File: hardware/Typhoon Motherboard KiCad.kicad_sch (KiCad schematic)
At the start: 51 parts, among them J1 Conn_01x04_Pin, J2 Conn_02x03_Odd_Even, J3 Conn_01x04_Pin, J4 Conn_01x02_Pin, J5 Conn_01x02_Pin, J6 Conn_01x02_Pin, J7 Conn_01x02_Pin, J8 Conn_01x02_Pin, J9 Conn_01x02_Pin, P1 USB_C_Plug_USB2.0, U1 ESP32-S3-WROOM-1, U2 TPS54331DDA, U3 TJA1051T-3, U7 MCP1825S

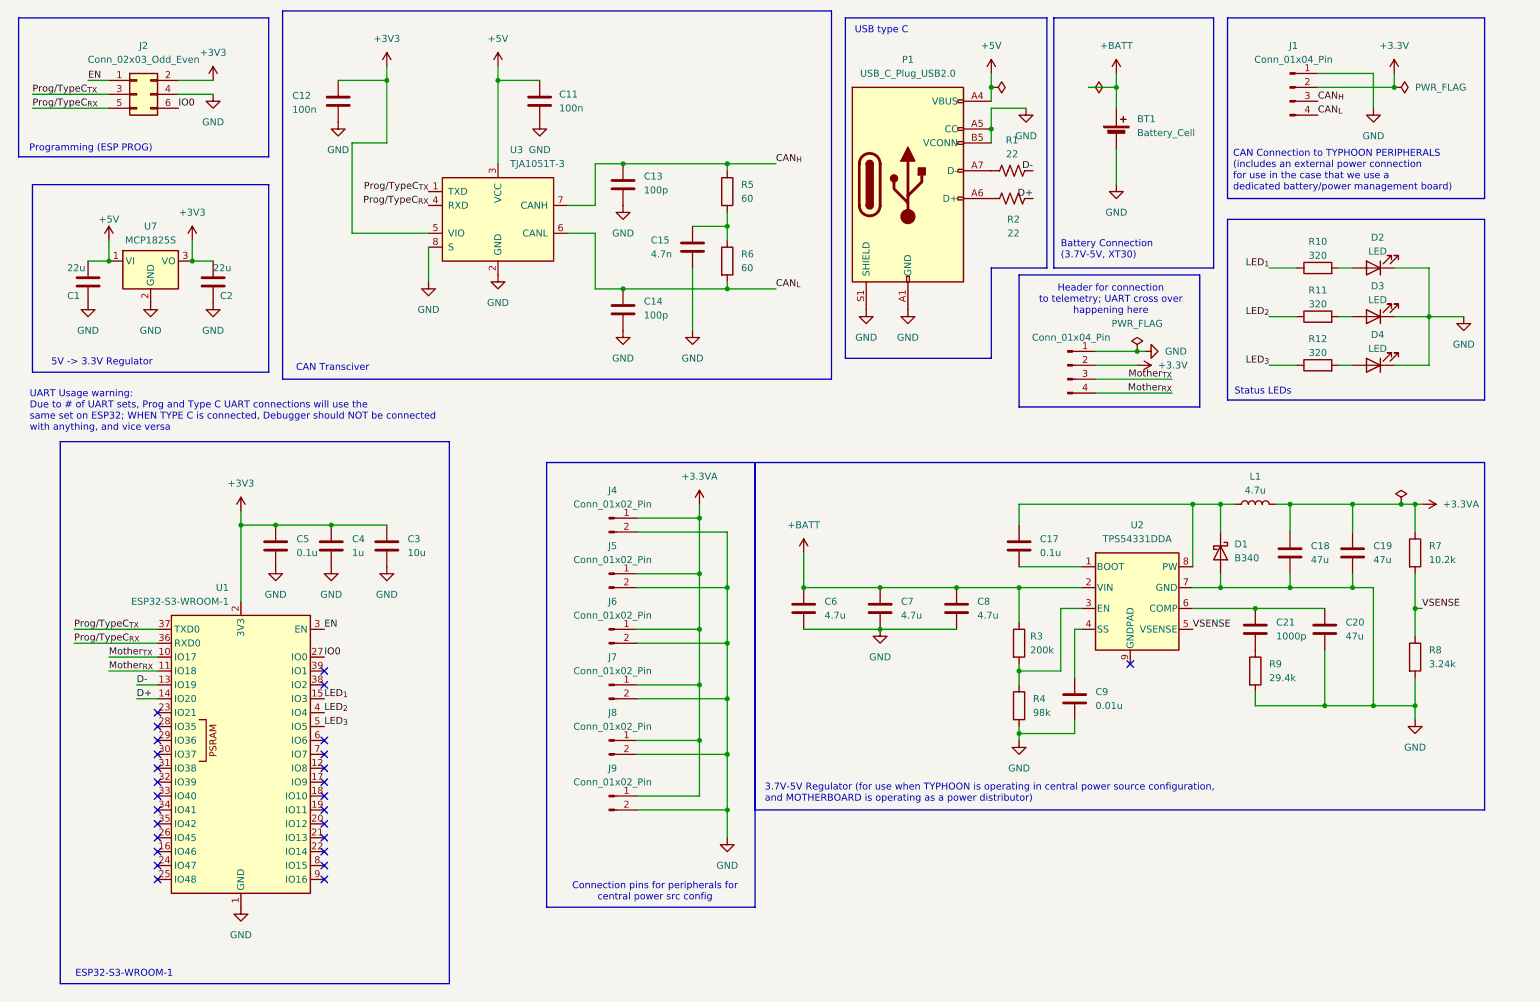
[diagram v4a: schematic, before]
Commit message: create new sheet; update USBC
created new sheet for the central power source configuration so it's more organized; updated the USB-C symbol; added in safety regulations (diodes) to prevent conflict in voltages
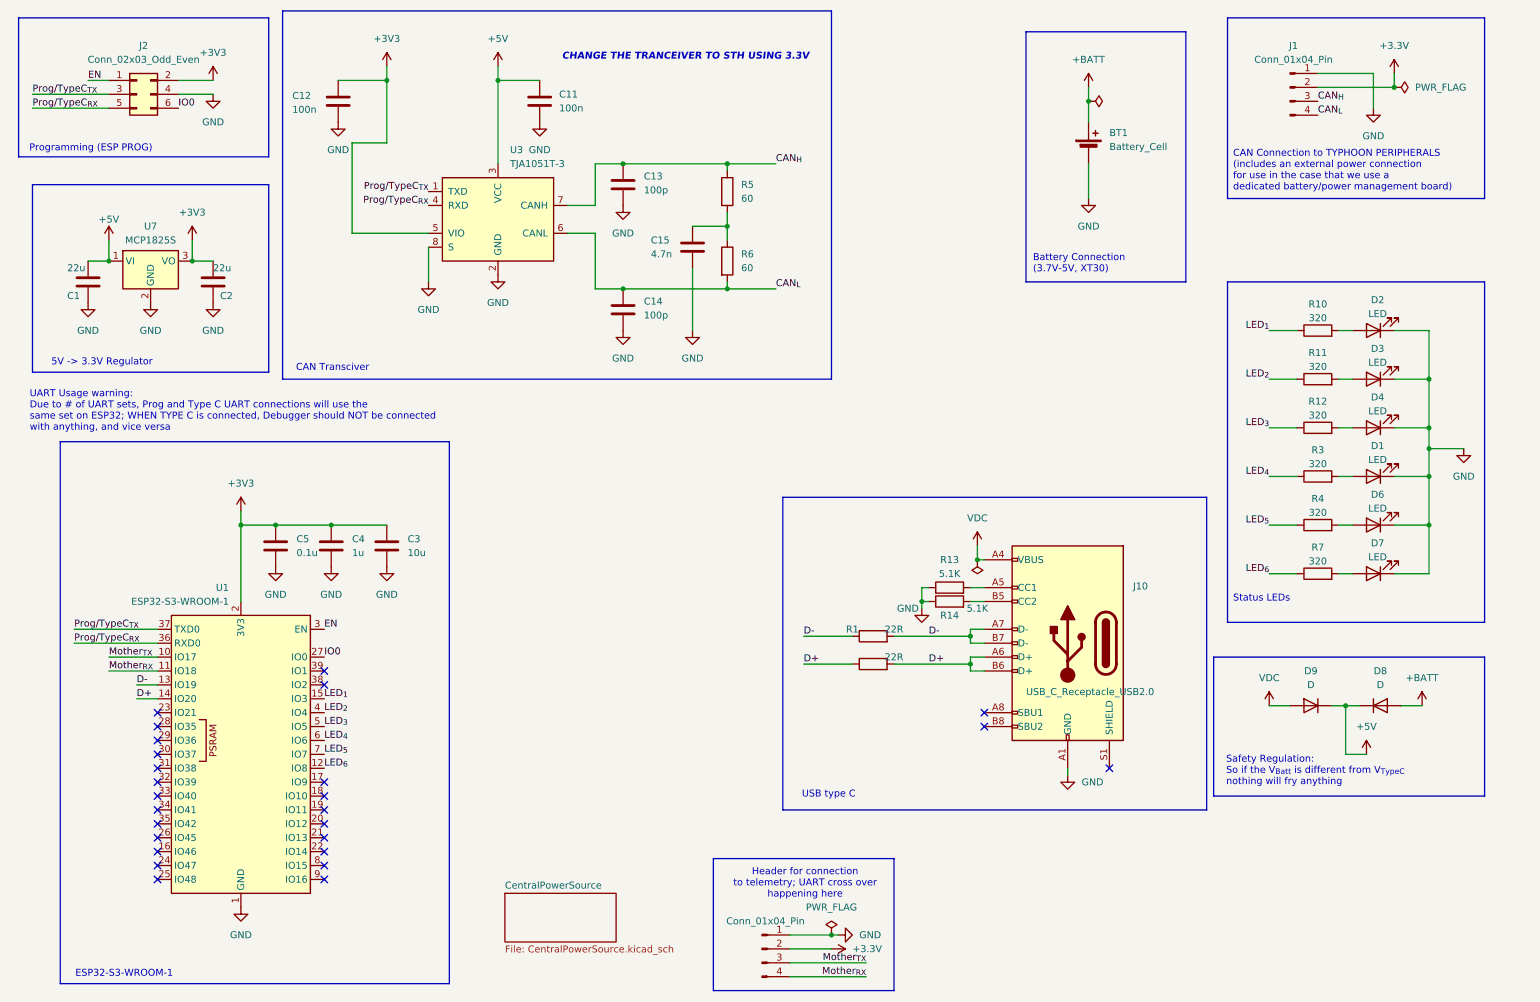
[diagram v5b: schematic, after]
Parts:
- removed C17: 0.1u, Capacitor_SMD:C_0603_1608Metric, symbol Device:C
- removed C18, C19, C20: 47u, Capacitor_SMD:C_0603_1608Metric, symbol Device:C
- removed C21: 1000p, Capacitor_SMD:C_0603_1608Metric, symbol Device:C
- removed C6, C7, C8: 4.7u, Capacitor_SMD:C_0603_1608Metric, symbol Device:C
- removed C9: 0.01u, Capacitor_SMD:C_0603_1608Metric, symbol Device:C
- removed D1: B340, Diode_SMD:D_SMC, symbol Diode:B340
- removed J4, J5, J6, J7, J8, J9: Conn_01x02_Pin, Connector_PinHeader_2.00mm:PinHeader_1x02_P2.00mm_Vertical_SMD_Pin1Right, symbol Connector:Conn_01x02_Pin
- removed L1: 4.7u, Inductor_SMD:L_Taiyo-Yuden_NR-60xx, symbol Device:L
- removed P1: USB_C_Plug_USB2.0, symbol Connector:USB_C_Plug_USB2.0
- removed R1, R2: 22, Resistor_SMD:R_0603_1608Metric, symbol Device:R_US
- removed R8: 3.24k, Resistor_SMD:R_0603_1608Metric, symbol Device:R
- removed R9: 29.4k, Resistor_SMD:R_0603_1608Metric, symbol Device:R
- removed U2: TPS54331DDA, Package_SO:TI_SO-PowerPAD-8_ThermalVias, symbol Regulator_Switching:TPS54360DDA
- added D1, D6, D7: LED, LED_SMD:LED_0805_2012Metric, symbol Device:LED
- added D8, D9: D, symbol Device:D
- added J10: USB_C_Receptacle_USB2.0, Connector_USB:USB_C_Receptacle_HRO_TYPE-C-31-M-12, symbol Connector:USB_C_Receptacle_USB2.0_16P
- added R1, R2: 22R, Resistor_SMD:R_0603_1608Metric, symbol Device:R
- added R13, R14: 5.1K, Resistor_SMD:R_0603_1608Metric, symbol Device:R
- R3: value 200k -> 320
- R4: value 98k -> 320
- R7: value 10.2k -> 320
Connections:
- net +3.3VA is gone; now on net LED_{6}: R7.1
- net +5V: now also D8.1 (K), D9.1 (K)
- net +BATT: now also D8.2 (A); no longer R3.1
- net D+: now also J10.A6 (D+), J10.B6 (D+), R2.1, R2.2
- net D-: now also J10.A7 (D-), J10.B7 (D-), R1.1, R1.2
- net GND: now also D1.1 (K), D6.1 (K), D7.1 (K), J10.A1 (GND), J10.A12 (GND), J10.B1 (GND), J10.B12 (GND), R13.1, R14.1; no longer R4.2
- net at R3.2: now also D1.2 (A); no longer R4.1
- net LED_{6}: now reaches U1.12 (IO8)
- net LED_{4}: now reaches U1.6 (IO6)
- net LED_{4}: now also R3.1
- net LED_{5}: now reaches U1.7 (IO7)
- net LED_{5}: now also R4.1
- net VSENSE: no longer names the net of R7.2
- net VSENSE: now also D7.2 (A)
- new net: J10.A5 (CC1), R13.2
- new net: J10.B5 (CC2), R14.2
- new net: D6.2 (A), R4.2
- new net VDC: D9.2 (A), J10.A4 (VBUS), J10.A9 (VBUS), J10.B4 (VBUS), J10.B9 (VBUS)
- no-connect marks 27 -> 26
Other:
- added sheet CentralPowerSource (CentralPowerSource.kicad_sch)
- note added: "CHANGE THE TRANCEIVER TO STH USING 3.3V"
- note added: "Safety Regulation: So if the V_{Batt} is different from V_{TypeC} nothing will fry anything"
- note removed: "3.7V-5V Regulator (for use when TYPHOON is operating in central power source configuration, and MOTHERBOARD is operating as a power distributor)"
- note removed: "Connection pins for peripherals for central power src config"
- moved on the sheet: BT1, D2, D3, D4, R10, R11, R12

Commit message: Everything written in the schematic
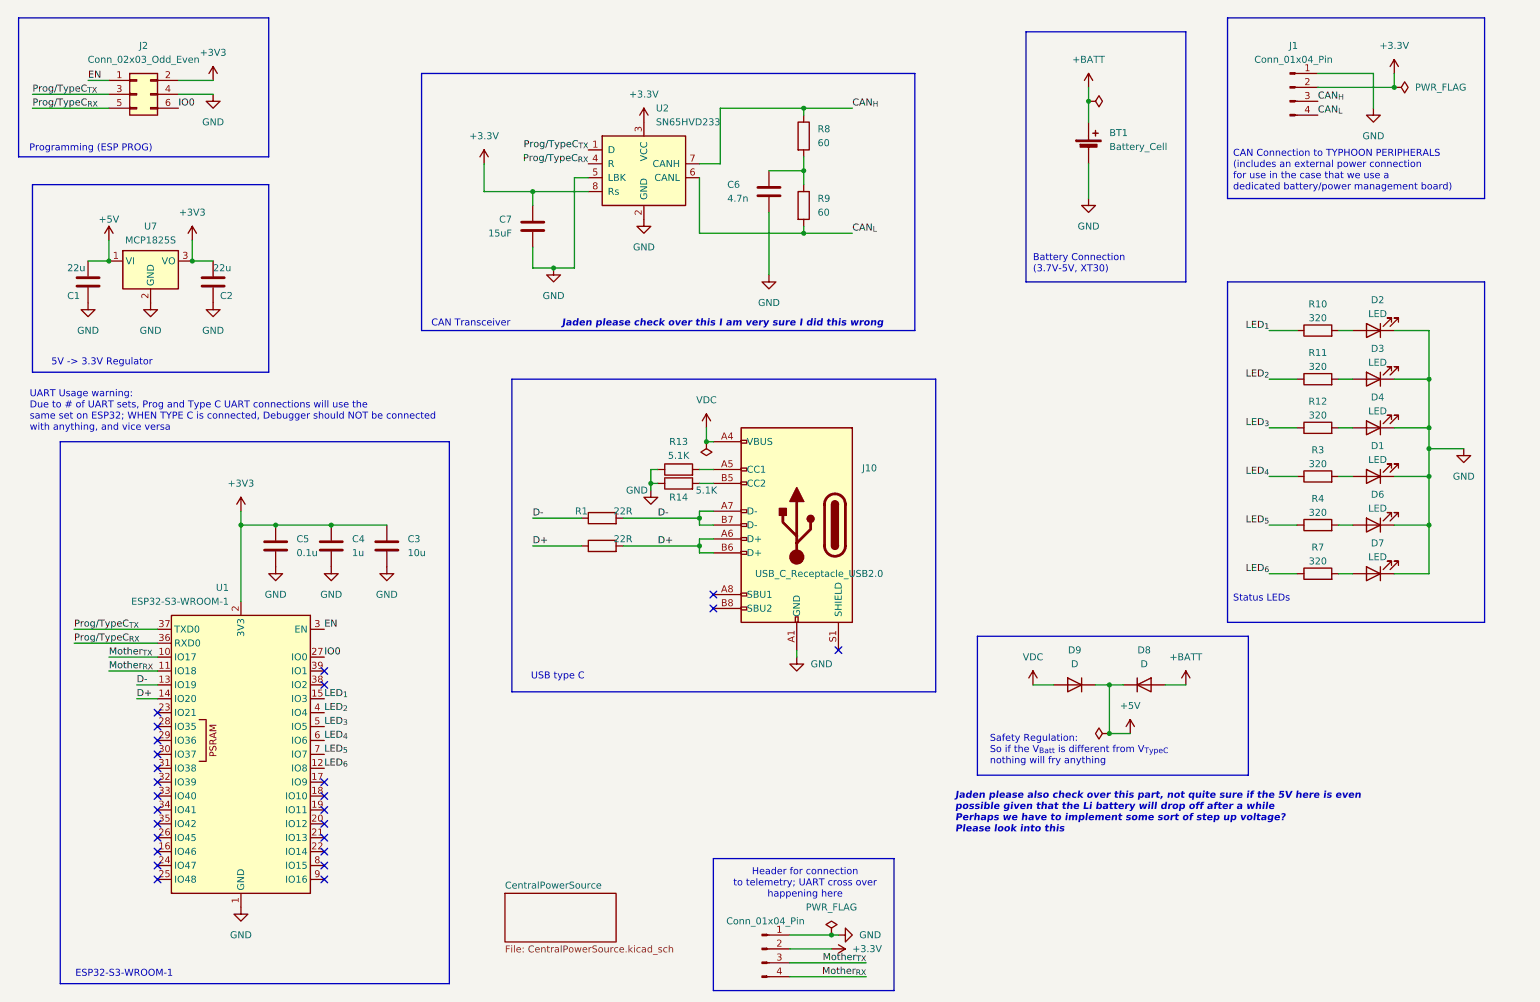
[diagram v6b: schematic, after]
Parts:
- removed C11, C12: 100n, Capacitor_SMD:C_0603_1608Metric, symbol Device:C
- removed C13, C14: 100p, Capacitor_SMD:C_0603_1608Metric, symbol Device:C
- removed C15: 4.7n, Capacitor_SMD:C_0603_1608Metric, symbol Device:C
- removed R5, R6: 60, Resistor_SMD:R_0603_1608Metric, symbol Device:R
- removed U3: TJA1051T-3, Package_SO:SOIC-8_3.9x4.9mm_P1.27mm, symbol Interface_CAN_LIN:TJA1051T-3
- added C6: 4.7n, Capacitor_SMD:C_0603_1608Metric, symbol Device:C
- added C7: 15uF, symbol Device:C
- added R8, R9: 60, Resistor_SMD:R_0603_1608Metric, symbol Device:R
- added U2: SN65HVD233, Package_SO:SOIC-8_3.9x4.9mm_P1.27mm, symbol Interface_CAN_LIN:SN65HVD233
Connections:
- net +3.3V: now also C7.1, U2.3 (VCC), U2.8 (Rs)
- net CAN_{H}: now also R8.1, U2.7 (CANH)
- net CAN_{L}: now also R9.2, U2.6 (CANL)
- net GND: now also C6.2, C7.2, U2.2 (GND), U2.5 (LBK)
- net Prog/TypeC_{RX}: now also U2.4 (R)
- net Prog/TypeC_{TX}: now also U2.1 (D)
- new net: C6.1, R8.2, R9.1
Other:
- note added: "CAN Transceiver"
- note added: "Jaden please also check over this part, not quite sure if the 5V here is even possible given that the Li battery will drop off after a while Perhaps we have to implement some sort of step up voltage? Please look into this"
- note added: "Jaden please check over this I am very sure I did this wrong"
- note removed: "CAN Transciver"
- note removed: "CHANGE THE TRANCEIVER TO STH USING 3.3V"
- moved on the sheet: D8, D9, J10, R1, R13, R14

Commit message: Update Schematics and Start PCB
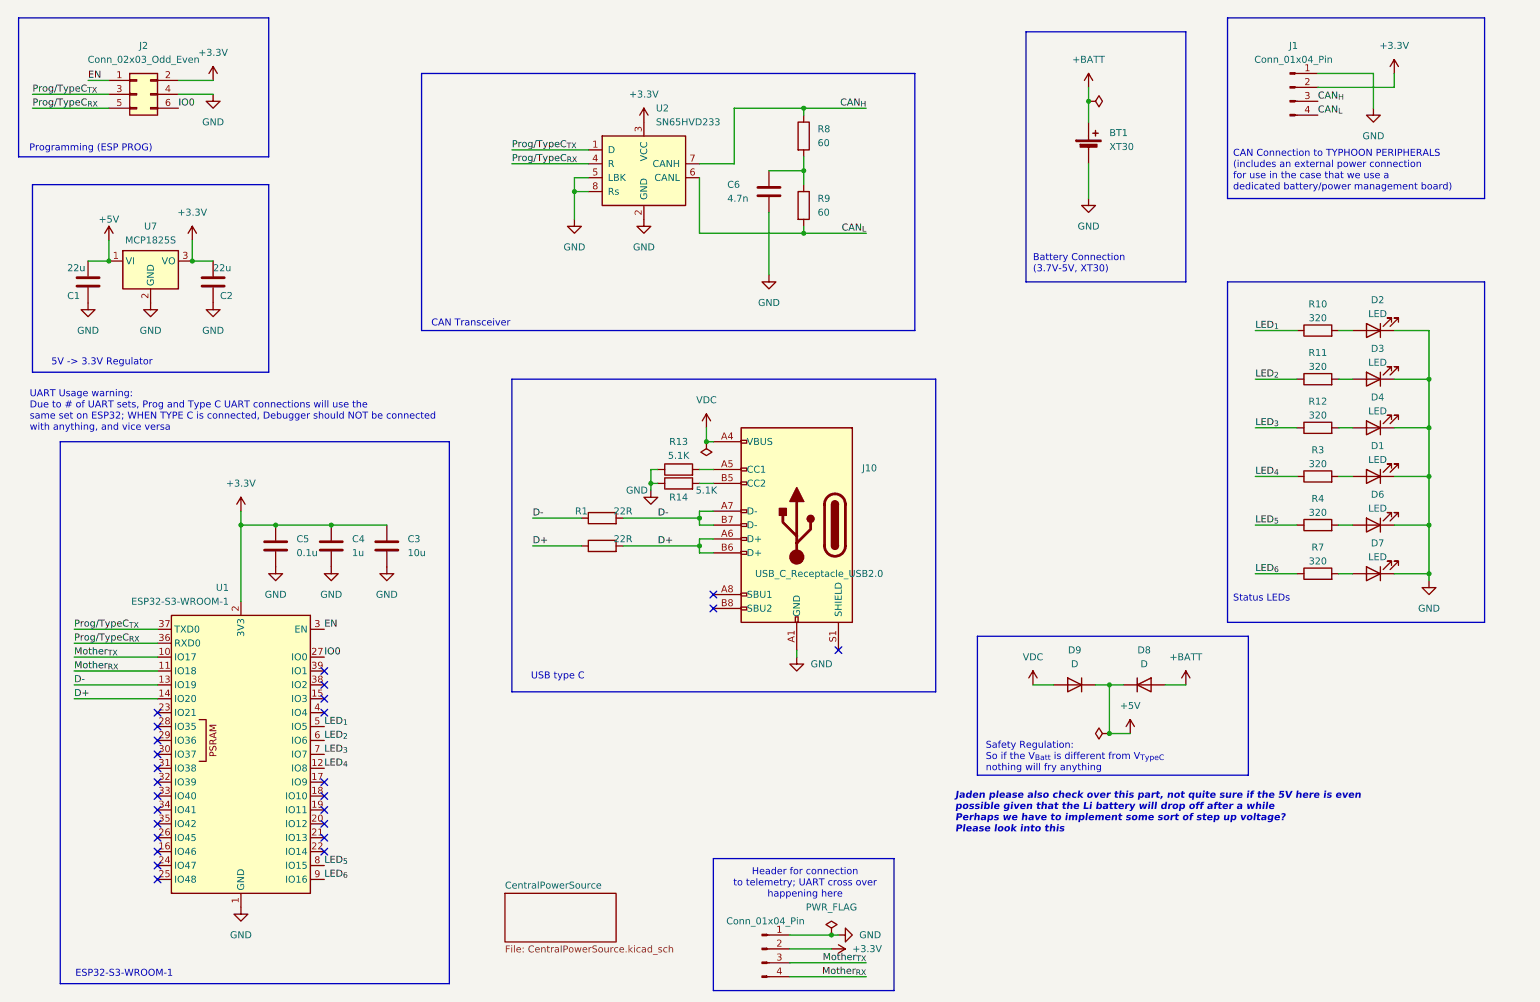
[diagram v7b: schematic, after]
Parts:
- removed C7: 15uF, symbol Device:C
- BT1: value Battery_Cell -> XT30
- D8, D9: footprint (none) -> Diode_SMD:D_SOD-123
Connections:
- net +3V3 is gone; now on net +3.3V: C2.2, C3.1, C4.1, C5.1, J2.2 (Pin_2), U1.2 (3V3), U7.3 (VO)
- net +3.3V: no longer U2.8 (Rs)
- net GND: now also U2.8 (Rs)
- net LED_{1}: now also U1.5 (IO5); no longer U1.15 (IO3)
- net LED_{2}: now also U1.6 (IO6); no longer U1.4 (IO4)
- net LED_{3}: now also U1.7 (IO7); no longer U1.5 (IO5)
- net LED_{4}: now also U1.12 (IO8); no longer U1.6 (IO6)
- net LED_{5}: now also U1.8 (IO15); no longer U1.7 (IO7)
- net LED_{6}: now also U1.9 (IO16); no longer U1.12 (IO8)
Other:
- note removed: "Jaden please check over this I am very sure I did this wrong"

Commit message: Updated header (NOT FINAL)
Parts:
- added H1, H2, H3, H4: M2.5, MountingHole:MountingHole_2.7mm_M2.5, symbol Mechanical:MountingHole
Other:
- note added: "Mounting Holes"
